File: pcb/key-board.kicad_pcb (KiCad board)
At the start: 2 copper layers, 21 x 30.2 mm, 4 parts

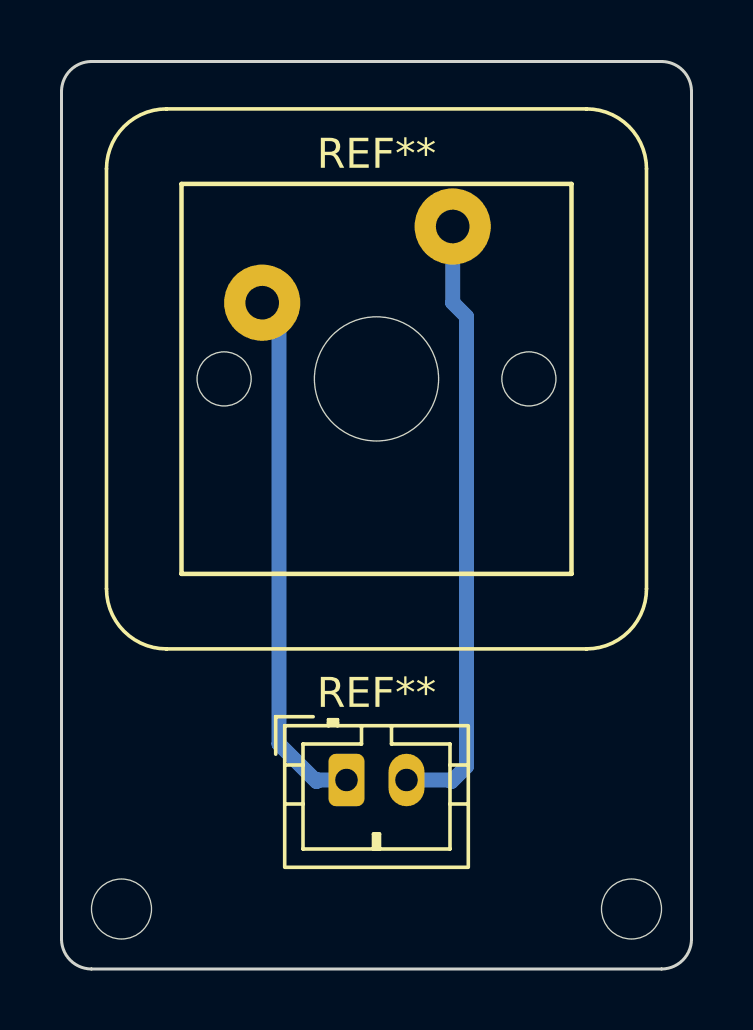
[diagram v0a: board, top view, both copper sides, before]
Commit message: add nc and chenge uf2 for studio
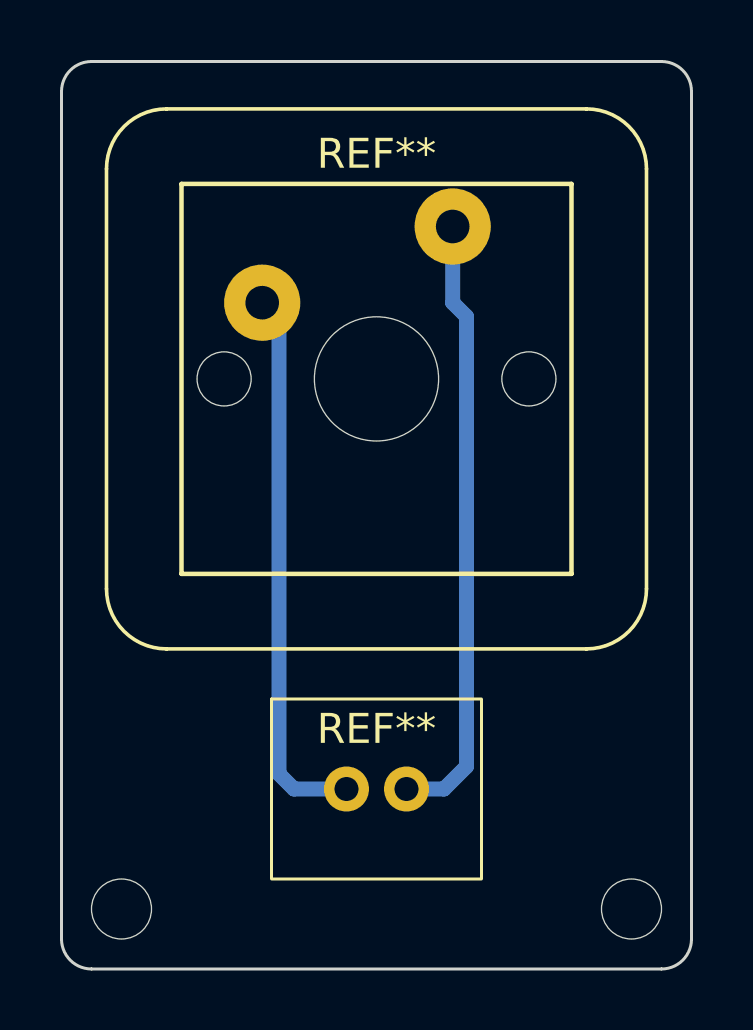
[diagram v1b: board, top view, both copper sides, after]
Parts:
- removed the REF** at (99.0, 88.5)
- added REF**: JST-PH-2-V, Suzuki:JstPh2Vertical, F.Cu at (100.0, 88.8)
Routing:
- net (no net): track 38.1 -> 38.9 mm
